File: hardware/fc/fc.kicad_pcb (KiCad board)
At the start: 4 copper layers, 42 x 41 mm, 96 parts, among them J1 USB-C, J10 GPIO, J11 BUZZER, J2 ESC, J3 ELRS, J4 I2C, J5 GPS, J6 VTX, J7 CAM, J8 SWD, J9 UART, Q1 Si2319CDS, Q2 2N7002, U1 STM32F405RGT6, U2 ICM-42688-P, U3 W25Q128JVSIQ, U4 LMR33630BDDA, U5 AMS1117-3.3, U6 USBLC6-2SC6, Y1 8MHz

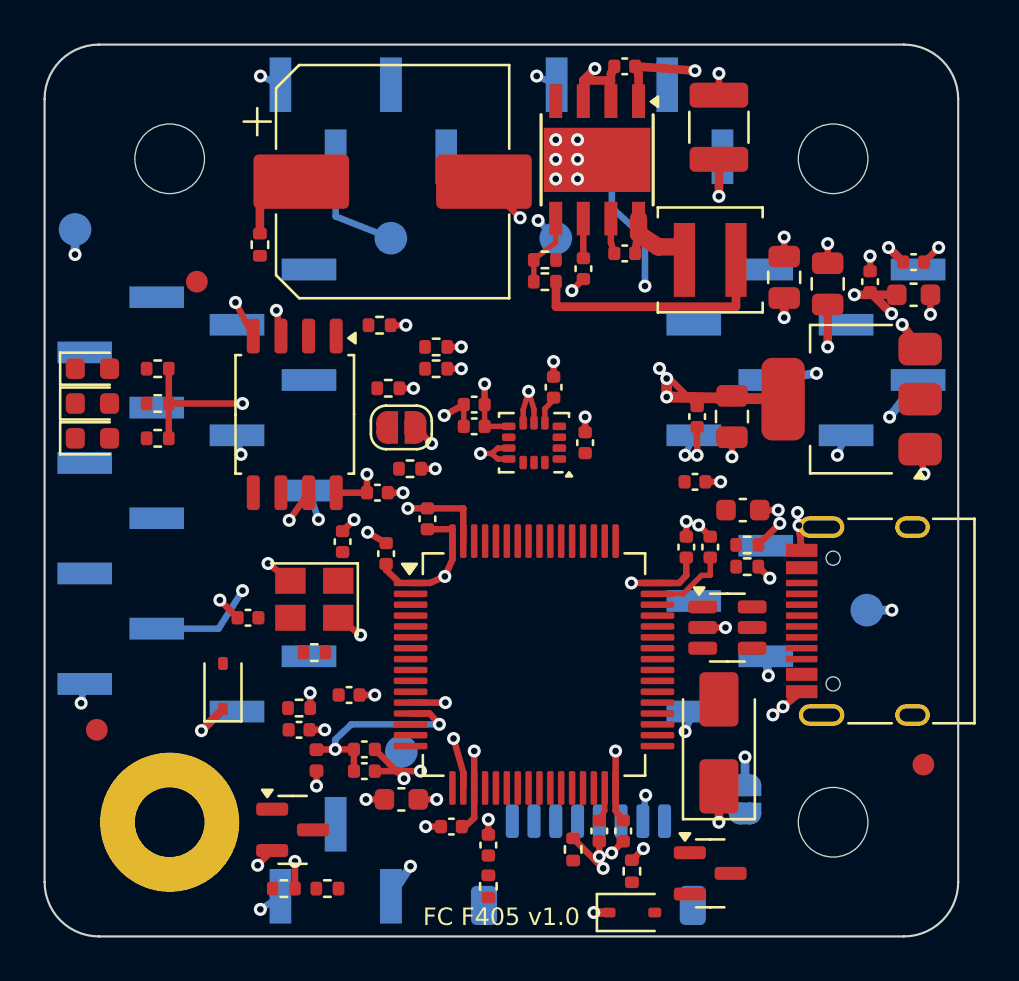
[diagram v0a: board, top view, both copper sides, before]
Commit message: FC-Hardware: vollständiges Routing, DRC sauber, JLCPCB-Fertigungsdaten
- Routing über alle vier Lagen: Handverdrahtung der kritischen Stellen
  (Abblockung, Schaltregler, USB-C/VBUS/CC, USB D+/D-, SPI-Bündel zum Gyro),
  Fanout in die Versorgungsflächen, Freerouting für die übrigen Signale,
  eigener Nachrouter (A*, mit Rip-up) für Restverbindungen
- Lage 2 durchgehend GND, Lage 3 VBAT/+5V/+3V3, außen GND-Restflächen
- DRC (KiCad 7.0.11): 0 Verstöße, 0 offene Verbindungen, 0 Footprint-Fehler;
  Platine <-> Schaltplan-Netzliste: 310 Pads, 0 Abweichungen
- GPIO4 auf PC5 verlegt (PA1 nicht entflechtbar), USB-C-Footprint mit an der
  Platinenkante gekürztem Bestückungsdruck
- Fertigung: Gerber, Excellon-Bohrdateien, ZIP, BOM und CPL im JLCPCB-Format
  (Ursprung linke untere Platinenecke)
- Doku: Schaltplan-PDF, Lagenbilder, DRC-Bericht, Routing-Kennzahlen,
  README mit unsicheren Stellen

Co-Authored-By: Claude Opus 5.5 <noreply@anthropic.com>
Claude-Session: https://claude.ai/code/session_01JZYB7PZbCVuDQ6ovPGKpbm
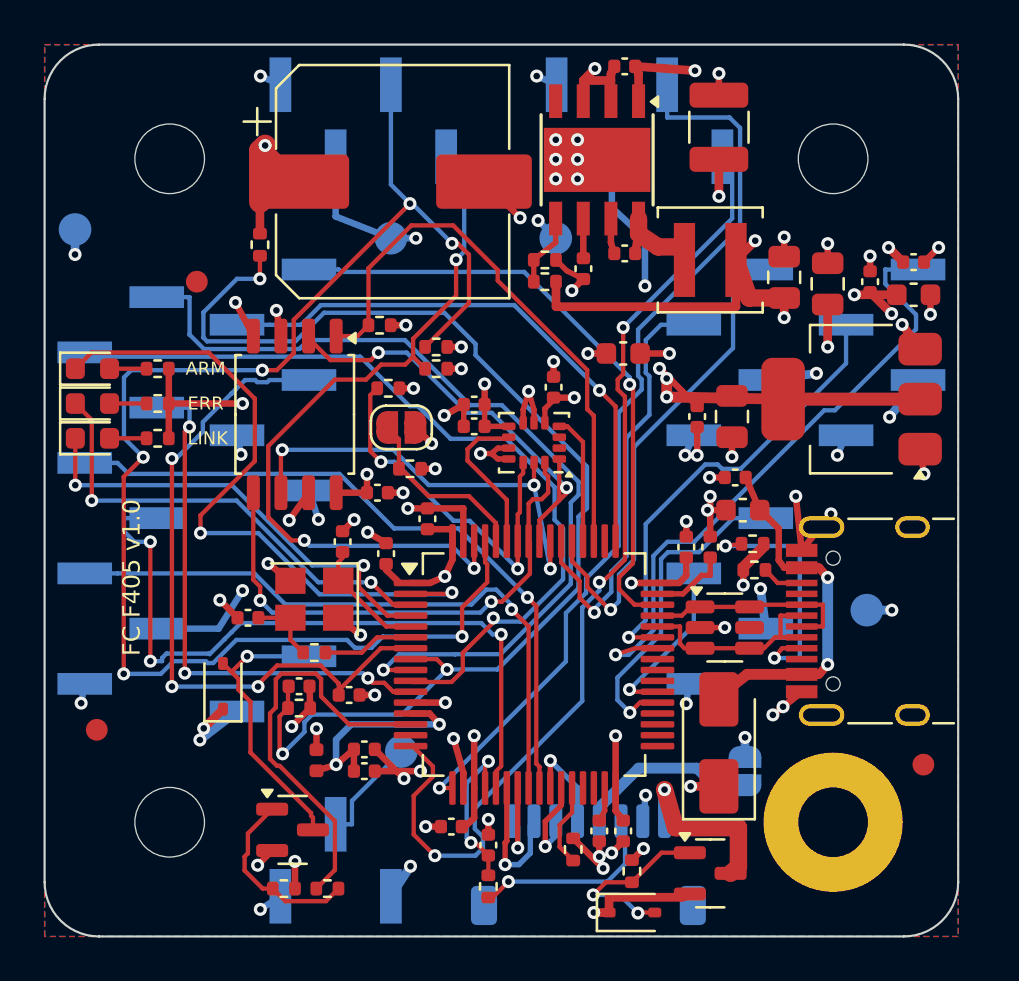
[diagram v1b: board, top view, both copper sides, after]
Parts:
- removed C19: 100nF, Capacitor_SMD:C_0402_1005Metric
- H1: value M3 GND -> M3; footprint MountingHole:MountingHole_3.2mm_M3_Pad -> MountingHole:MountingHole_3.2mm_M3
- H2: value M3 -> M3 GND; footprint MountingHole:MountingHole_3.2mm_M3 -> MountingHole:MountingHole_3.2mm_M3_Pad
- J1: footprint Connector_USB:USB_C_Receptacle_HRO_TYPE-C-31-M-12 -> fc_custom:USB_C_Receptacle_HRO_TYPE-C-31-M-12_Kante
- moved C6 22.9 mm to (105.6, 93.7)
- moved C14 2.00 mm to (90.7, 109.0)
- moved C34 1.86 mm to (110.8, 99.4), turned to 180 degrees
- moved JP2 1.30 mm to (111.2, 112.9)
- moved J6 1.27 mm to (110.5, 105.1)
- moved R13 0.36 mm to (111.6, 103.7), turned to 180 degrees
- moved R12 0.25 mm to (111.5, 102.5)
- moved U6 0.12 mm to (110.3, 106.3)
- turned C33 to 180 degrees
- turned FB1 to -90 degrees
- turned J11 to 0 degrees
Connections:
- U1 pad 15: GPIO4 -> (no net)
- U1 pad 25: (no net) -> GPIO4
- U2 pad 2: GYRO_RESV -> (no net)
- U6 pad 5: VBUS -> (no net)
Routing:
- net I2C_SCL: track 0.00 -> 67.9 mm, vias 0 -> 6
- net VBAT_SENSE: track 0.00 -> 54.9 mm, vias 0 -> 3
- net DBG_TX: track 0.00 -> 45.3 mm, vias 0 -> 3
- net DBG_RX: track 0.00 -> 41.9 mm, vias 0 -> 1
- net GPIO1: track 0.00 -> 40.6 mm, vias 0 -> 1
- net GPIO2: track 0.00 -> 37.9 mm, vias 0 -> 1
- net I2C_SDA: track 0.00 -> 34.6 mm, vias 0 -> 3
- net GPIO5: track 0.00 -> 32.6 mm, vias 0 -> 3
- net GPIO4: track 0.00 -> 31.9 mm, vias 0 -> 1
- net NRST: track 0.00 -> 31.6 mm, vias 0 -> 3
- net LED_ARM: track 0.00 -> 31.3 mm, vias 0 -> 2
- net GPIO6: track 0.00 -> 29.5 mm, vias 0 -> 1
- net SWDIO: track 0.00 -> 28.9 mm, vias 0 -> 1
- net ELRS_TX: track 0.00 -> 28.9 mm, vias 0 -> 1
- net FLASH_CS: track 0.00 -> 26.2 mm
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- added copper zone on B.Cu, net GND
- added copper zone on F.Cu, net GND
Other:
- board text added: "ARM"
- board text added: "ERR"
- board text added: "LINK"

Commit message: FC: JLCPCB-Bestückung vorbereitet (LCSC-Nummern, CPL-Drehlagen, ERC)
- scripts/lcsc.py: LCSC-Nummer für alle 71 Bauteile der Oberseite, Typ
  Basic/Preferred/Extended nach der JLCPCB-Liste vom 13.10.2026, Bestand mit
  Datum und Quelle; 11 Extended-Teile, 4 Preferred
- Stückliste getrennt: jlcpcb_bom.csv / jlcpcb_cpl.csv (Oberseite, maschinell),
  handbestueckung_unten.csv (Steckverbinder J2-J11)
- CPL mit Drehkorrektur (Tabelle JLCKicadTools) und Prüfliste mit Lage von
  Pin 1 bzw. Kathode/Pluspol je Bauteil; LGA-14 und HSOP-8 ohne Tabellenwert
- Basic statt Extended: 5-V-Rückführung 33k/8,2k (5,02 V) statt 100k/24,9k;
  R16 470 Ohm für die grüne InGaN-LED; Quarz CL 12 pF passend zu 18 pF
- Werte und LCSC-Felder in Schaltplan und Platine (sync_fields.py, Kupfer
  unverändert); DRC 0/0, Abgleich Platine/Schaltplan 0 Abweichungen
- ERC mit KiCad 9.0.3: 0 Fehler, 2 Warnungen (Flash /WP und /HOLD an 3,3 V)
- README: Bestellhinweise Economic PCBA, Extended-Liste, J2-Prüfung

Co-Authored-By: Claude Opus 5.5 <noreply@anthropic.com>
Claude-Session: https://claude.ai/code/session_01JZYB7PZbCVuDQ6ovPGKpbm
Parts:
- R10: value 100k -> 33k
- R11: value 24.9k -> 8.2k
- R16: value 1k -> 470R
